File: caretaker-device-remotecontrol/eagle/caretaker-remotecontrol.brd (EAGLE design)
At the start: 50 x 100 mm, 50 parts, among them IC1 MAX1811N, IC2 ATMEGA168, IC3 XBee Series 2, IC4 ZLDO330, K1 BAT, K2 ISP, K3 USB-MINIB-5PIN, Q1 16MHz

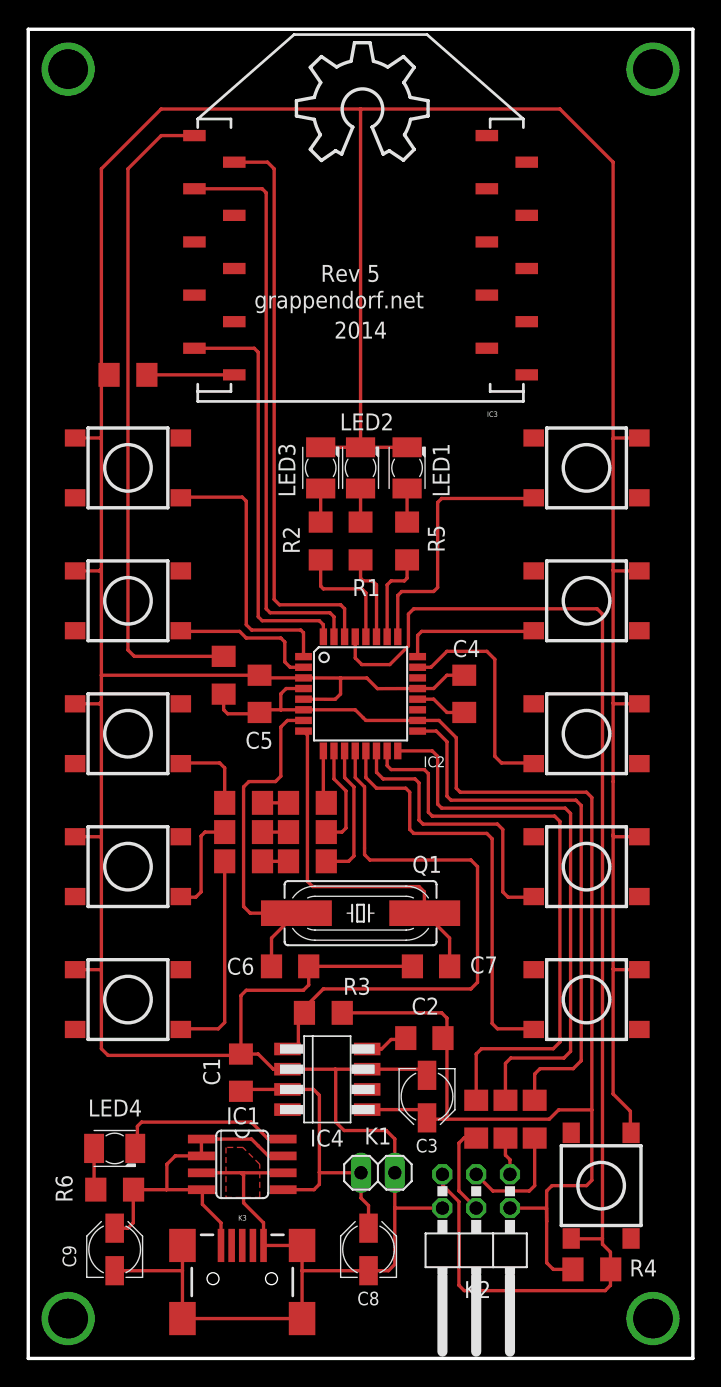
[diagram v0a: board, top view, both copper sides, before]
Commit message: feat: Convert the XBee RemoteControl device to a WLAN device
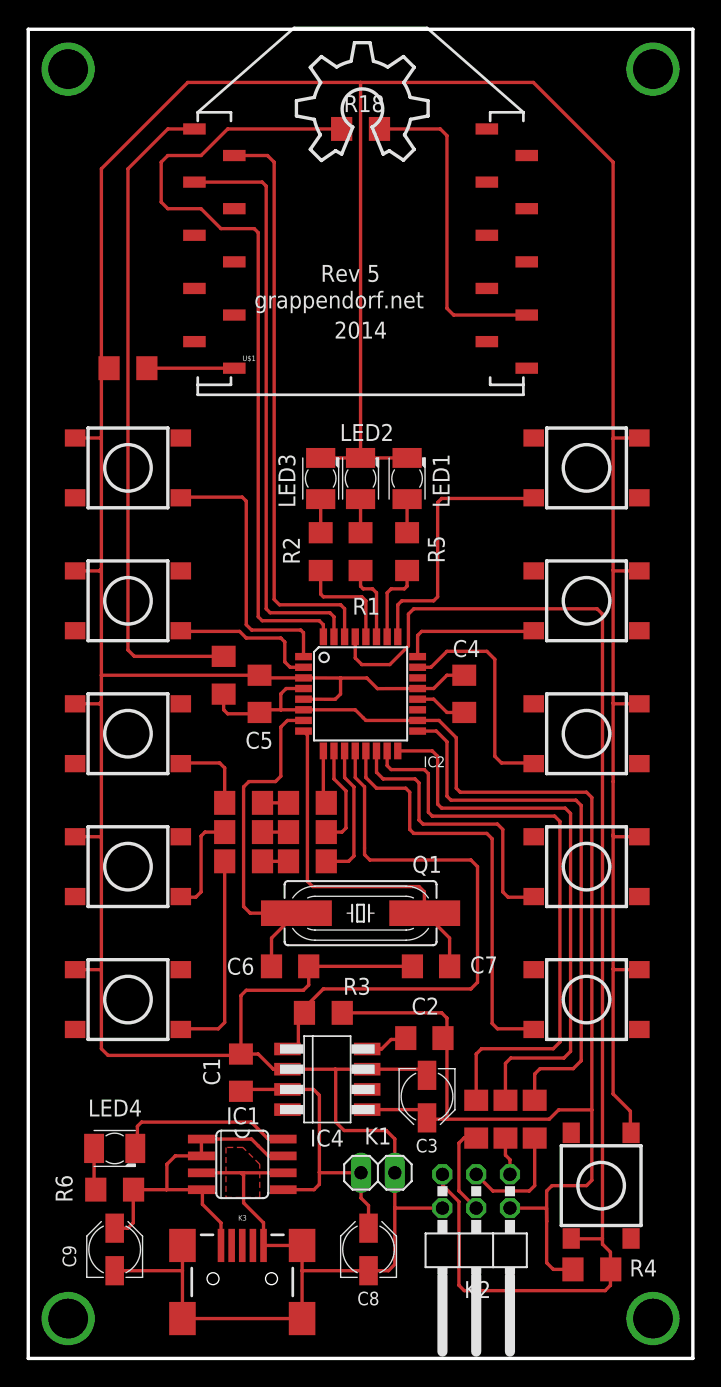
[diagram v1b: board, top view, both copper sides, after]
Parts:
- removed IC3: XBee Series 2, grapelabs:XBEE-SMD
- added R18: 0, rcl:R1206
- added U$1: WIFLY-SMD, grapelabs:WIFLY-SMD
- moved LED1 0.80 mm to (28.5, 66.2)
- moved LED2 0.80 mm to (25.0, 66.2)
- moved LED3 0.80 mm to (22.0, 66.2)
- moved R1 0.80 mm to (25.0, 60.7)
- moved R2 0.80 mm to (22.0, 60.7)
- moved R5 0.80 mm to (28.5, 60.7)
- moved R13 0.50 mm to (7.50, 74.5)
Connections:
- removed net XBEESLEEP: IC2.32, IC3.9
- new net N$27: R18.2, U$1.13
- new net WIFLYSLEEP: IC2.32, R18.1
- net N$22: now also U$1.10; no longer IC3.10
- net N$23: now also U$1.1; no longer IC3.1
- net RXD: now also U$1.2; no longer IC3.2
- net TXD: now also U$1.3; no longer IC3.3
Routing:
- net WIFLYSLEEP: track 0.00 -> 60.8 mm
- net XBEESLEEP: track 30.9 -> 0.00 mm
- net N$27: track 0.00 -> 24.5 mm
- net GND: track 382.0 -> 387.0 mm
- net LED3: track 8.89 -> 8.09 mm
- net LED2: track 6.69 -> 5.89 mm
- net LED1: track 6.99 -> 6.19 mm
- net TXD: track 43.7 -> 44.2 mm
- net RXD: track 43.3 -> 43.8 mm
